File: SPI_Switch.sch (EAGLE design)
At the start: 44 parts, among them J1 8516-4500PL, J2 1-406525-1, J3 1-406525-1, J4 0705510037, J5 0705510037, U1 TLE7230G, U2 SN74ABT126

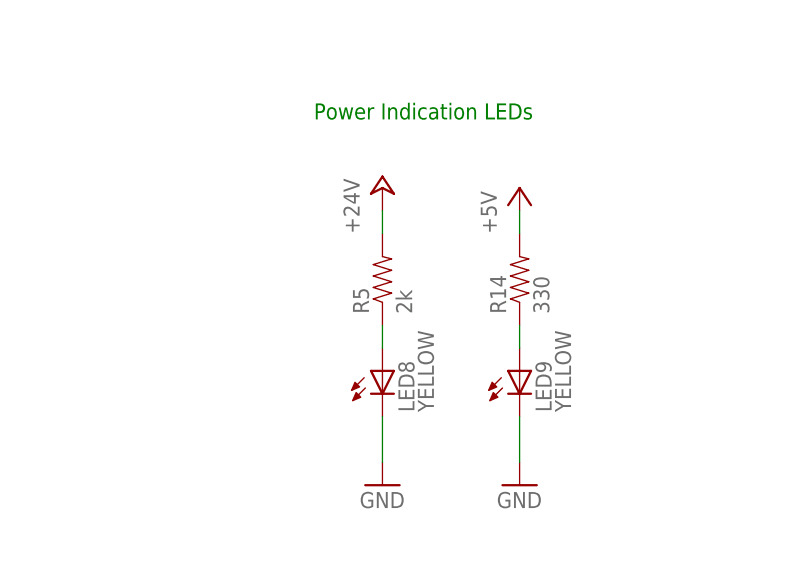
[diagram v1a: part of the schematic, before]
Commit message: Switched the footprint for R5 to be smaller
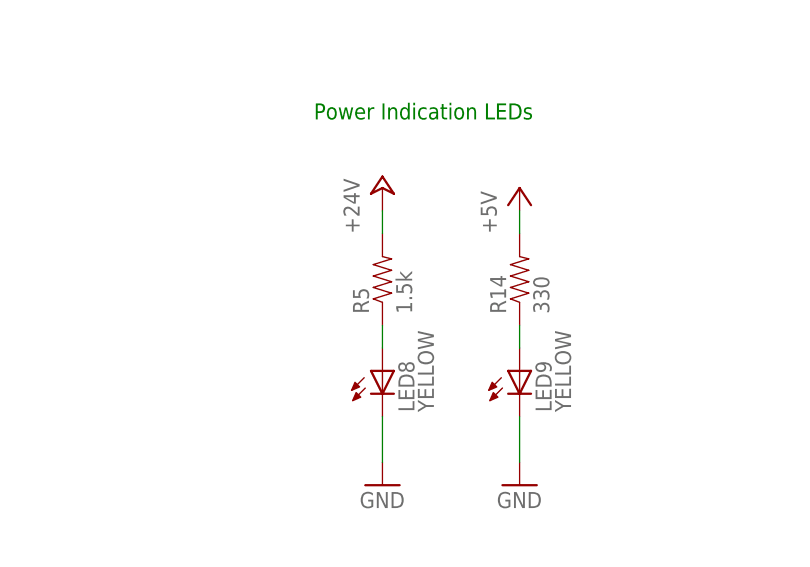
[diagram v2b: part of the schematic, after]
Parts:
- R5: value 2k -> 1.5k; device SparkFun-Passives:RESISTOR2512 -> SparkFun-Passives:RESISTOR1206
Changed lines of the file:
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@@
 <part name="LED9" library="SparkFun-LED" deviceset="LED" device="1206" value="YELLOW"/>
 <part name="P+19" library="supply1" deviceset="+5V" device=""/>
-<part name="R5" library="SparkFun-Passives" deviceset="RESISTOR" device="2512" value="2k"/>
 <part name="R14" library="SparkFun-Passives" deviceset="RESISTOR" device="0805-RES" value="330"/>
 <part name="C1" library="SparkFun-Passives" deviceset="CAP" device="0805" value="10uF"/>
@@
 <part name="H3" library="holes" deviceset="MOUNT-HOLE" device="2.8"/>
 <part name="H4" library="holes" deviceset="MOUNT-HOLE" device="2.8"/>
+<part name="R5" library="SparkFun-Passives" deviceset="RESISTOR" device="1206" value="1.5k"/>
 </parts>
 <sheets>
@@
 <instance part="LED9" gate="G$1" x="96.52" y="353.06"/>
 <instance part="P+19" gate="1" x="96.52" y="373.38"/>
-<instance part="R5" gate="G$1" x="81.28" y="363.22" rot="R90"/>
 <instance part="R14" gate="G$1" x="96.52" y="363.22" rot="R90"/>
 <instance part="C1" gate="G$1" x="81.28" y="302.26"/>
@@
 <instance part="H3" gate="G$1" x="58.42" y="228.6"/>
 <instance part="H4" gate="G$1" x="58.42" y="223.52"/>
+<instance part="R5" gate="G$1" x="81.28" y="363.22" rot="R90"/>
 </instances>
 <busses>
